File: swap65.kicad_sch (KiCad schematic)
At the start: 34 parts, among them J1 USB_C_Receptacle_USB2.0, SW1 SW_Push, SW2 SW_Push, U1 RP2040, U2 USBLC6-2SC6, U3 XC6206PxxxMR, U4 W25Q128JVS, Y1 12MHz

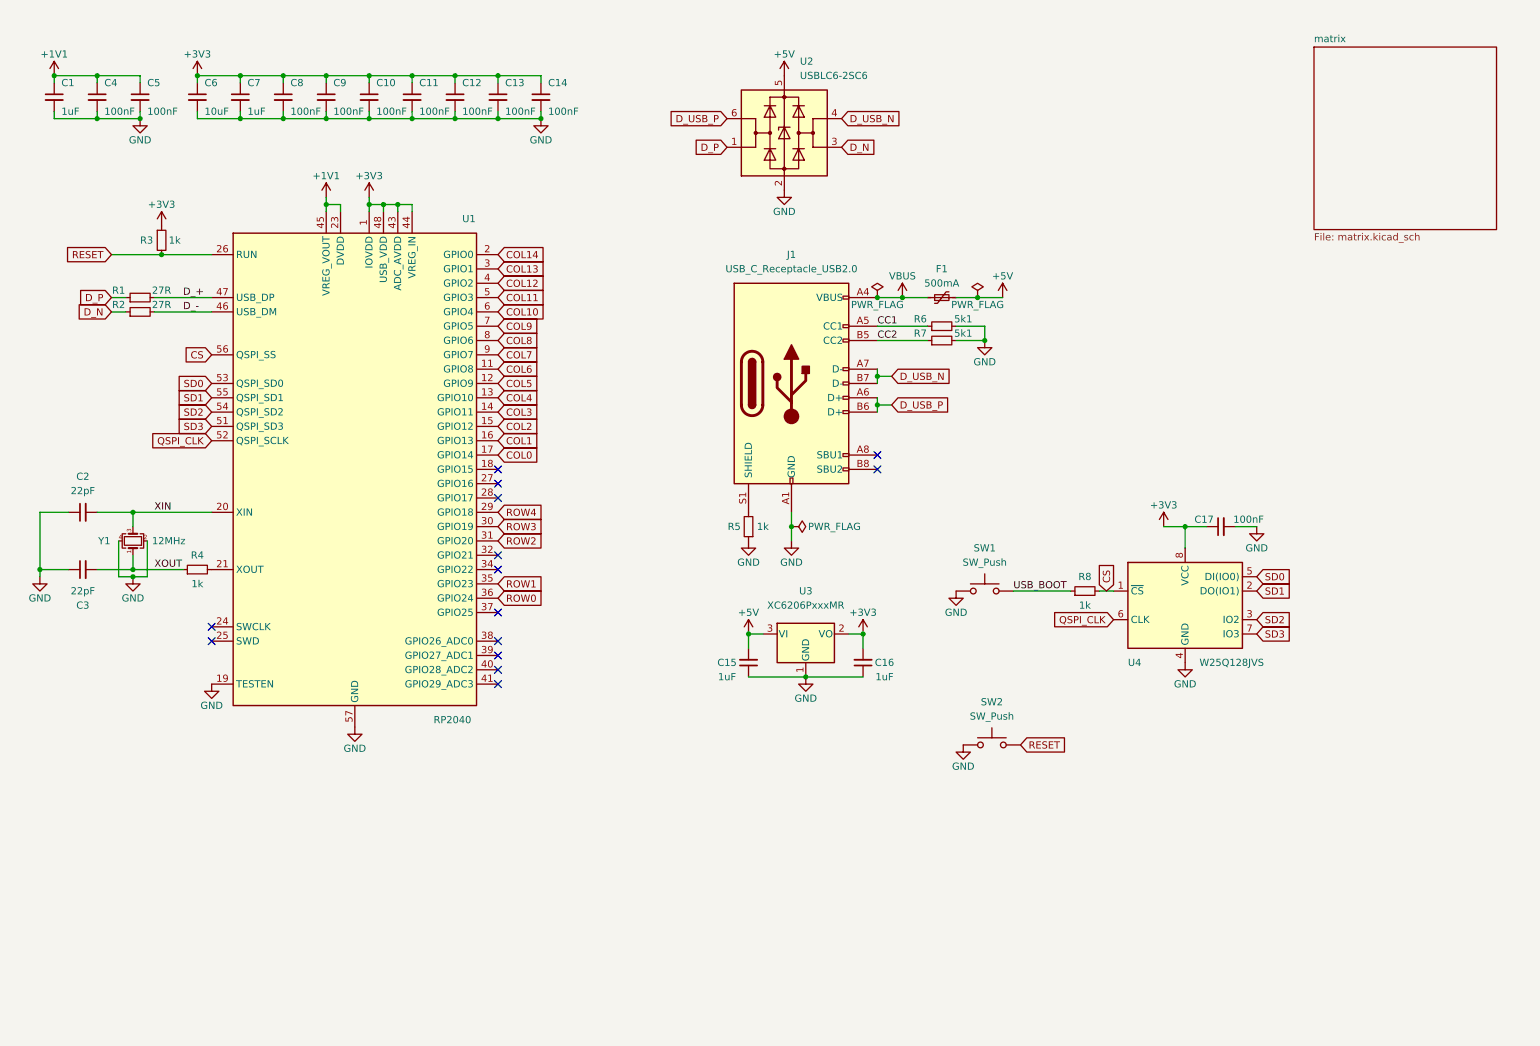
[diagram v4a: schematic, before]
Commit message: added screen header to schematic
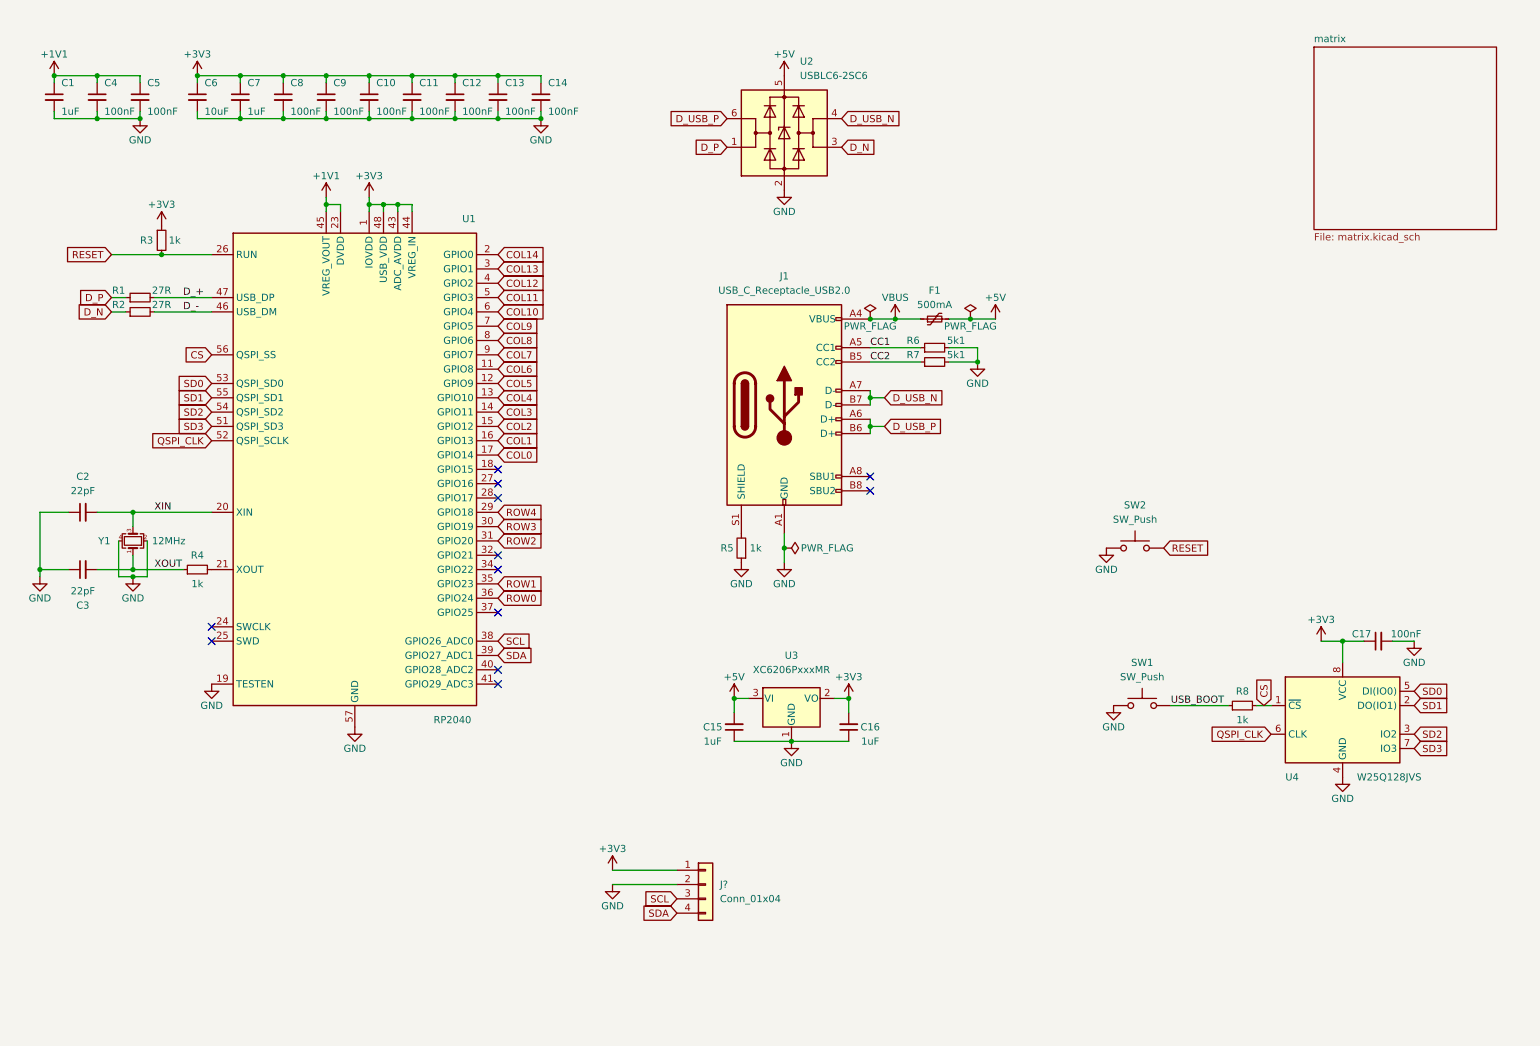
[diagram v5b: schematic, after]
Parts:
- added J?: Conn_01x04, symbol Connector_Generic:Conn_01x04
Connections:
- net +3V3: now also J?.1 (Pin_1)
- net GND: now also J?.2 (Pin_2)
- net SCL: now reaches U1.38 (GPIO26_ADC0)
- net SCL: now also J?.3 (Pin_3)
- net SDA: now reaches U1.39 (GPIO27_ADC1)
- net SDA: now also J?.4 (Pin_4)
- no-connect marks 14 -> 12
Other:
- moved on the sheet: C15, C16, C17, F1, J1, R5, R6, R7, R8, SW1, SW2, U3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

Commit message: completed route pass 1
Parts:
- J2: renamed from J?; value Conn_01x04 -> OLED; footprint (none) -> Connector_PinHeader_2.54mm:PinHeader_1x04_P2.54mm_Vertical
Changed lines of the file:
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@@
   (symbol (lib_id "power:+3V3") (at 120.65 166.37 0) (unit 1)
     (in_bom yes) (on_board yes)
-    (property "Reference" "#PWR?" (id 0) (at 120.65 170.18 0)
+    (property "Reference" "#PWR0102" (id 0) (at 120.65 170.18 0)
       (effects (font (size 1.27 1.27)) hide)
     )
@@
   (symbol (lib_id "Connector_Generic:Conn_01x04") (at 137.16 168.91 0) (unit 1)
     (in_bom yes) (on_board yes) (fields_autoplaced)
-    (property "Reference" "J?" (id 0) (at 139.7 168.9099 0)
-      (effects (font (size 1.27 1.27)) (justify left))
-    )
-    (property "Value" "Conn_01x04" (id 1) (at 139.7 171.4499 0)
-      (effects (font (size 1.27 1.27)) (justify left))
-    )
-    (property "Footprint" "" (id 2) (at 137.16 168.91 0)
+    (property "Reference" "J2" (id 0) (at 139.7 168.9099 0)
+      (effects (font (size 1.27 1.27)) (justify left))
+    )
+    (property "Value" "OLED" (id 1) (at 139.7 171.4499 0)
+      (effects (font (size 1.27 1.27)) (justify left))
+    )
+    (property "Footprint" "Connector_PinHeader_2.54mm:PinHeader_1x04_P2.54mm_Vertical" (id 2) (at 137.16 168.91 0)
       (effects (font (size 1.27 1.27)) hide)
     )
@@
   (symbol (lib_id "power:GND") (at 120.65 168.91 0) (unit 1)
     (in_bom yes) (on_board yes)
-    (property "Reference" "#PWR?" (id 0) (at 120.65 175.26 0)
+    (property "Reference" "#PWR0101" (id 0) (at 120.65 175.26 0)
       (effects (font (size 1.27 1.27)) hide)
     )
@@
       (reference "#PWR026") (unit 1) (value "GND") (footprint "")
     )
+    (path "/e68f93c6-1525-499e-acec-0db2bf143259"
+      (reference "#PWR0101") (unit 1) (value "GND") (footprint "")
+    )
     (path "/2a41ba2a-9949-4df2-bdeb-f252c396cedf"
-      (reference "#PWR?") (unit 1) (value "+3V3") (footprint "")
-    )
-    (path "/e68f93c6-1525-499e-acec-0db2bf143259"
-      (reference "#PWR?") (unit 1) (value "GND") (footprint "")
+      (reference "#PWR0102") (unit 1) (value "+3V3") (footprint "")
     )
     (path "/520bad3e-5c36-4559-91de-edb06e0e641d"
@@
     )
     (path "/cae0e1b1-9487-46db-ad2c-ad47579ebd8e"
-      (reference "J?") (unit 1) (value "Conn_01x04") (footprint "")
+      (reference "J2") (unit 1) (value "OLED") (footprint "Connector_PinHeader_2.54mm:PinHeader_1x04_P2.54mm_Vertical")
     )
     (path "/5906767e-3e7f-41b3-9f1a-a9d001e4281d"
@@
     )
     (path "/4c22d526-8605-498d-80f5-ad20d643781f/1d7ddbff-5ac7-4929-b748-ee085871cee8"
-      (reference "SW60") (unit 1) (value "Pipe") (footprint "marbastlib-mx:SW_MX_HS_1u")
+      (reference "SW60") (unit 1) (value "Pipe") (footprint "marbastlib-mx:SW_MX_HS_S_1u")
     )
     (path "/4c22d526-8605-498d-80f5-ad20d643781f/b465f019-40c2-4a51-8a6d-73645fc8ad9e"
@@
     )
     (path "/4c22d526-8605-498d-80f5-ad20d643781f/52a34629-ad18-49b1-8e85-6dc3f19bf2f8"
-      (reference "SW65") (unit 1) (value "BkSpc") (footprint "marbastlib-mx:SW_MX_HS_1u")
+      (reference "SW65") (unit 1) (value "BkSpc") (footprint "marbastlib-mx:SW_MX_HS_S_1u")
     )
     (path "/4c22d526-8605-498d-80f5-ad20d643781f/cfe80bc2-b293-419e-8d17-f3727aa786f1"
-      (reference "SW66") (unit 1) (value "Tilde") (footprint "marbastlib-mx:SW_MX_HS_1u")
+      (reference "SW66") (unit 1) (value "Tilde") (footprint "marbastlib-mx:SW_MX_HS_S_1u")
     )
     (path "/4c22d526-8605-498d-80f5-ad20d643781f/06084a08-d138-48af-bb7a-e47886851923"

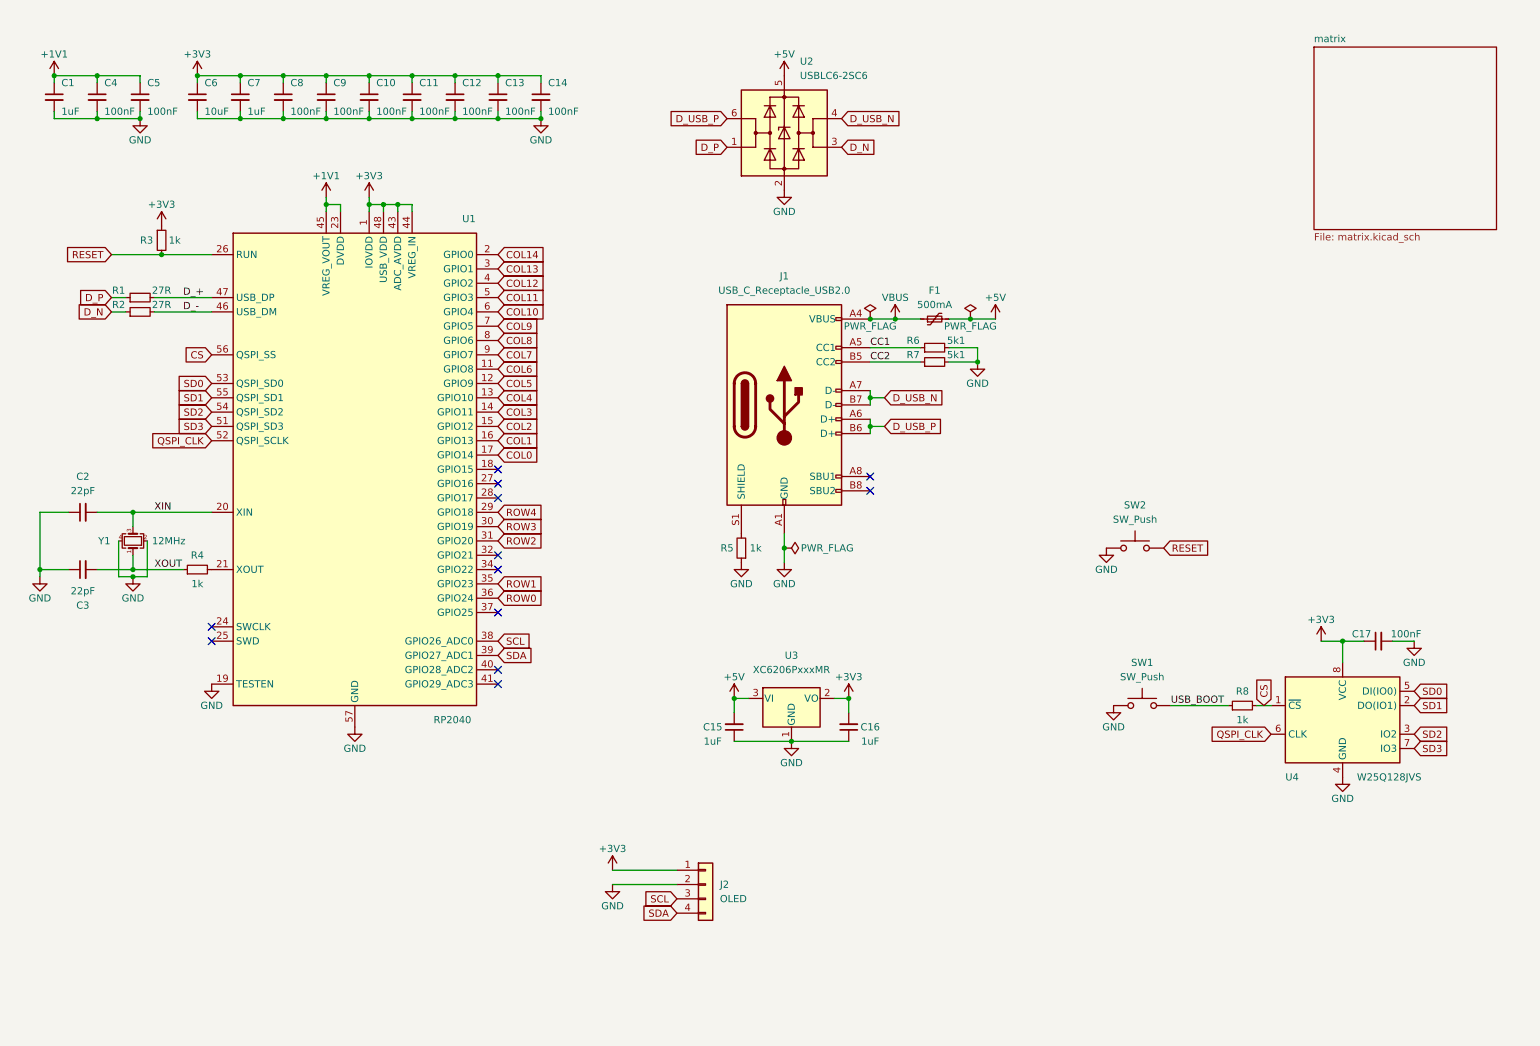
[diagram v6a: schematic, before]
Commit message: organized schematic
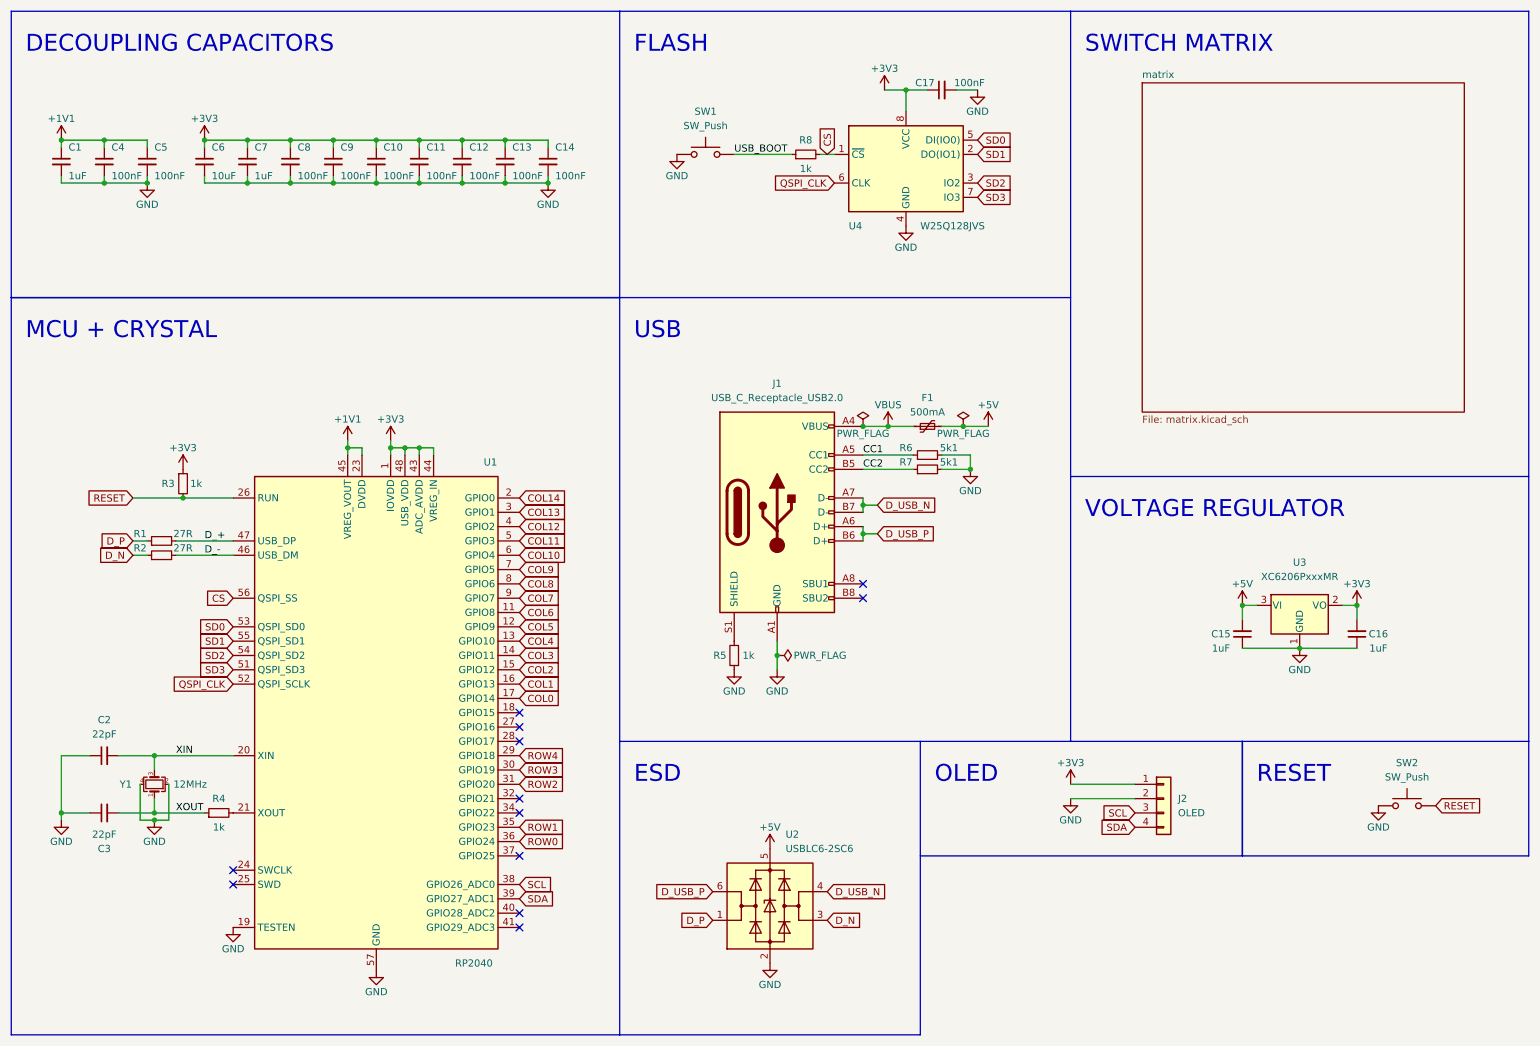
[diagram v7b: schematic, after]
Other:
- note added: "DECOUPLING CAPACITORS"
- note added: "ESD"
- note added: "FLASH"
- note added: "MCU + CRYSTAL"
- note added: "OLED"
- note added: "RESET"
- note added: "SWITCH MATRIX"
- note added: "USB"
- note added: "VOLTAGE REGULATOR"
- moved on the sheet: C1, C10, C11, C12, C13, C14, C15, C16, C17, C2, C3, C4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

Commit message: swapped USD to basic part and added db jst connector
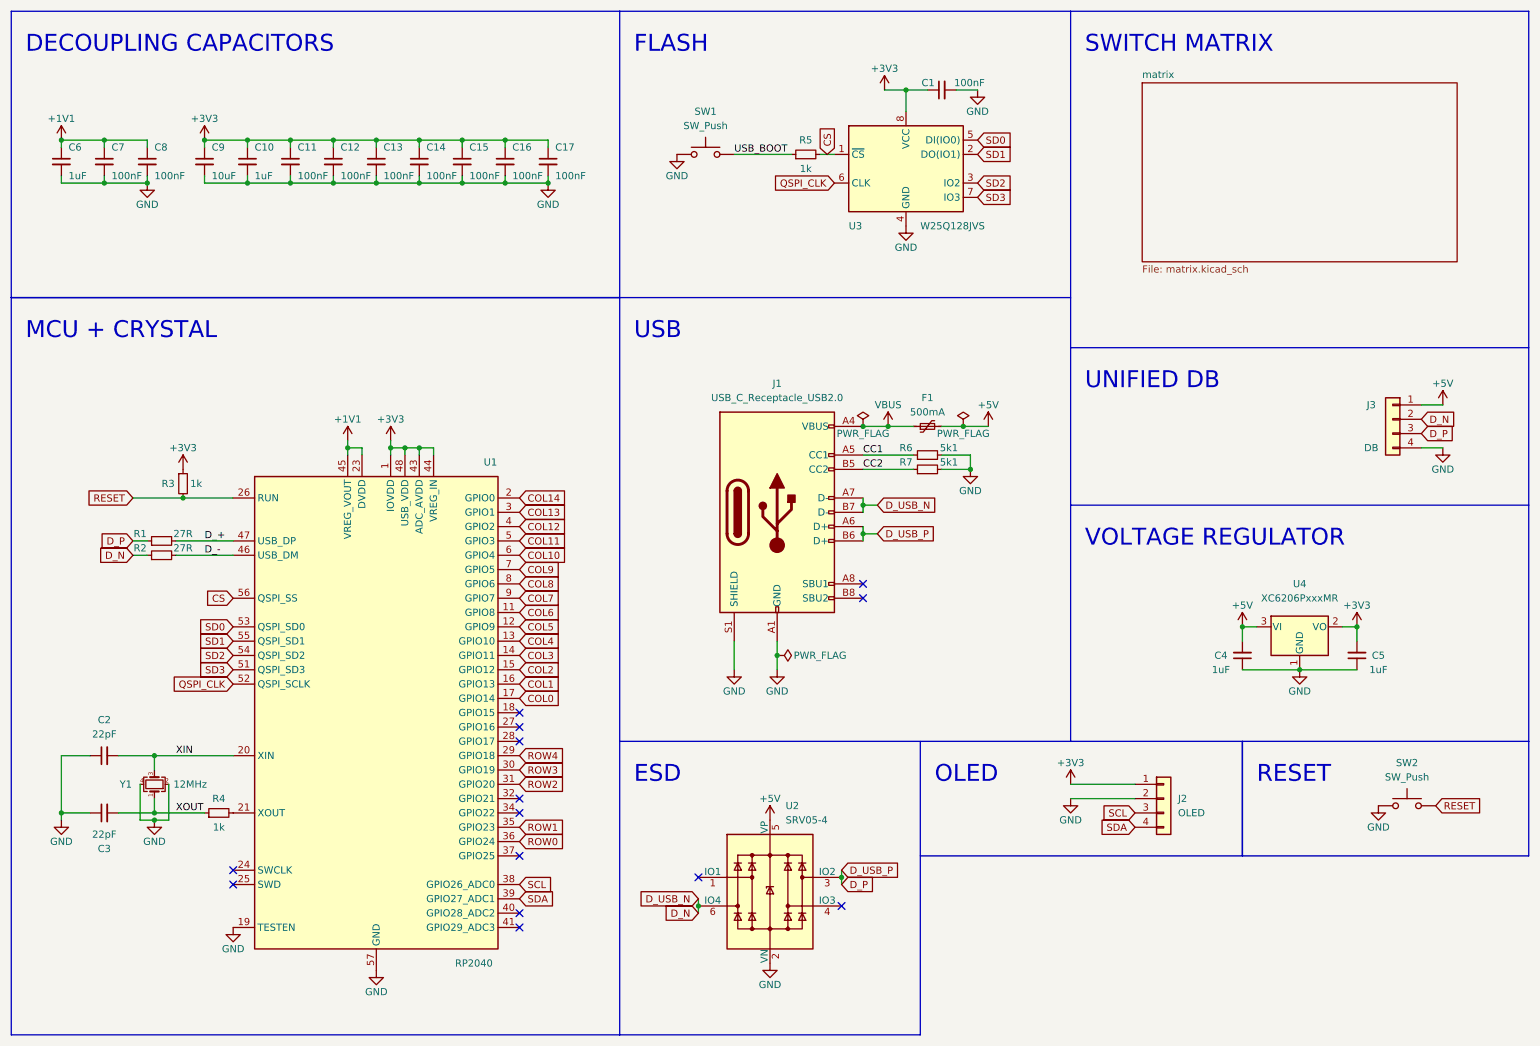
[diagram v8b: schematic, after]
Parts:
- removed R5: 1k, Resistor_SMD:R_0402_1005Metric_Pad0.72x0.64mm_HandSolder, symbol Device:R_Small
- removed U2: USBLC6-2SC6, Package_TO_SOT_SMD:SOT-23-6, symbol Power_Protection:USBLC6-2SC6
- added J3: DB, Connector_JST:JST_SH_SM04B-SRSS-TB_1x04-1MP_P1.00mm_Horizontal, symbol Connector_Generic:Conn_01x04
- added U2: SRV05-4, marbastlib-various:SOT-23-6-routable, symbol marbastlib-various:SRV05-4
- renumbered C17 to C1, C7 to C10, C8 to C11, C9 to C12, C10 to C13, C11 to C14, C12 to C15, C13 to C16, C14 to C17, C15 to C4, C16 to C5, C1 to C6, C4 to C7, C5 to C8, C6 to C9, R8 to R5, U4 to U3, U3 to U4
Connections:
- net D_USB_N is gone; now on net D_N: J1.A7 (D-), J1.B7 (D-)
- net D_USB_P is gone; now on net D_P: J1.A6 (D+), J1.B6 (D+)
- net +5V: now also J3.1 (Pin_1), U2.5 (VP)
- net D_N: now also J3.2 (Pin_2), U2.6 (IO4)
- net D_P: now also J3.3 (Pin_3), U2.3 (IO2)
- net GND: now also J1.S1 (SHIELD), J3.4 (Pin_4), U2.2 (VN)
- no-connect marks 12 -> 14
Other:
- note added: "UNIFIED DB"
- moved on the sheet: C4, C5, U4
